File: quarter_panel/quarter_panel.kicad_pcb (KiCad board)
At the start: 2 copper layers, 20 x 20 mm, 4 parts

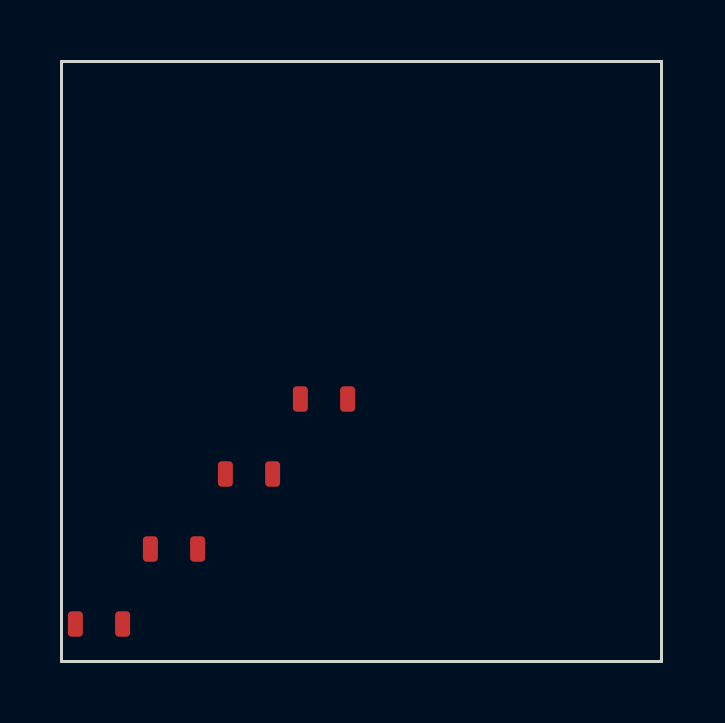
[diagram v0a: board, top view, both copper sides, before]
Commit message: Create new documentation images
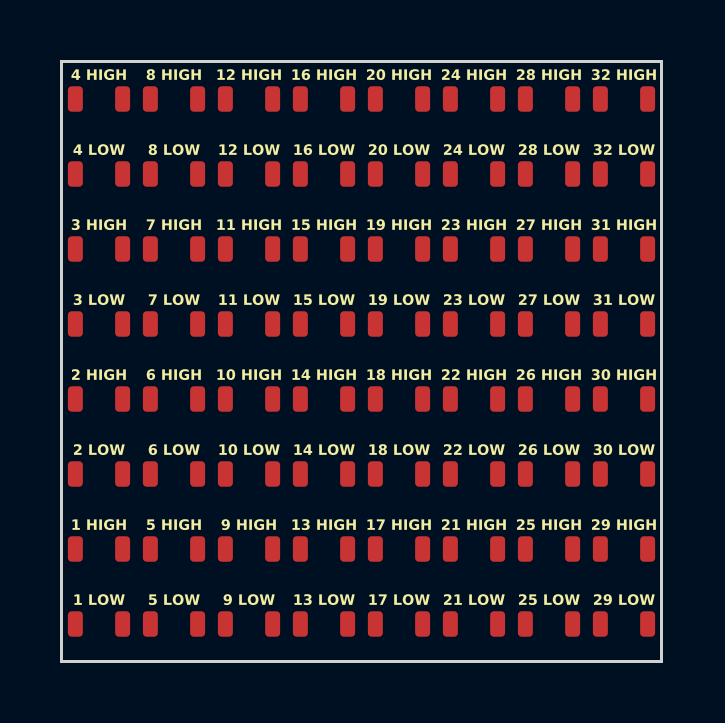
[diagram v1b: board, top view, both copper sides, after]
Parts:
- added REF**: LED_0603_1608Metric, LED_SMD:LED_0603_1608Metric, F.Cu at (128.8, 106.2)
- added REF**: LED_0603_1608Metric, LED_SMD:LED_0603_1608Metric, F.Cu at (138.8, 111.2)
- added REF**: LED_0603_1608Metric, LED_SMD:LED_0603_1608Metric, F.Cu at (138.8, 116.2)
- added REF**: LED_0603_1608Metric, LED_SMD:LED_0603_1608Metric, F.Cu at (131.2, 103.8)
- added REF**: LED_0603_1608Metric, LED_SMD:LED_0603_1608Metric, F.Cu at (143.8, 118.8)
- added REF**: LED_0603_1608Metric, LED_SMD:LED_0603_1608Metric, F.Cu at (143.8, 113.8)
- added REF**: LED_0603_1608Metric, LED_SMD:LED_0603_1608Metric, F.Cu at (133.8, 108.8)
- added REF**: LED_0603_1608Metric, LED_SMD:LED_0603_1608Metric, F.Cu at (128.8, 101.2)
- added REF**: LED_0603_1608Metric, LED_SMD:LED_0603_1608Metric, F.Cu at (136.2, 111.2)
- added REF**: LED_0603_1608Metric, LED_SMD:LED_0603_1608Metric, F.Cu at (131.2, 111.2)
- added REF**: LED_0603_1608Metric, LED_SMD:LED_0603_1608Metric, F.Cu at (138.8, 101.2)
- added REF**: LED_0603_1608Metric, LED_SMD:LED_0603_1608Metric, F.Cu at (133.8, 116.2)
- added REF**: LED_0603_1608Metric, LED_SMD:LED_0603_1608Metric, F.Cu at (141.2, 106.2)
- added REF**: LED_0603_1608Metric, LED_SMD:LED_0603_1608Metric, F.Cu at (131.2, 116.2)
- added REF**: LED_0603_1608Metric, LED_SMD:LED_0603_1608Metric, F.Cu at (143.8, 101.2)
- added REF**: LED_0603_1608Metric, LED_SMD:LED_0603_1608Metric, F.Cu at (143.8, 111.2)
- added REF**: LED_0603_1608Metric, LED_SMD:LED_0603_1608Metric, F.Cu at (133.8, 113.8)
- added REF**: LED_0603_1608Metric, LED_SMD:LED_0603_1608Metric, F.Cu at (143.8, 103.8)
- added REF**: LED_0603_1608Metric, LED_SMD:LED_0603_1608Metric, F.Cu at (143.8, 116.2)
- added REF**: LED_0603_1608Metric, LED_SMD:LED_0603_1608Metric, F.Cu at (126.2, 111.2)
- added REF**: LED_0603_1608Metric, LED_SMD:LED_0603_1608Metric, F.Cu at (133.8, 118.8)
- added REF**: LED_0603_1608Metric, LED_SMD:LED_0603_1608Metric, F.Cu at (126.2, 103.8)
- added REF**: LED_0603_1608Metric, LED_SMD:LED_0603_1608Metric, F.Cu at (141.2, 103.8)
- added REF**: LED_0603_1608Metric, LED_SMD:LED_0603_1608Metric, F.Cu at (131.2, 118.8)
- added REF**: LED_0603_1608Metric, LED_SMD:LED_0603_1608Metric, F.Cu at (128.8, 103.8)
- added REF**: LED_0603_1608Metric, LED_SMD:LED_0603_1608Metric, F.Cu at (141.2, 116.2)
- added REF**: LED_0603_1608Metric, LED_SMD:LED_0603_1608Metric, F.Cu at (143.8, 106.2)
- added REF**: LED_0603_1608Metric, LED_SMD:LED_0603_1608Metric, F.Cu at (131.2, 101.2)
- added REF**: LED_0603_1608Metric, LED_SMD:LED_0603_1608Metric, F.Cu at (141.2, 113.8)
- added REF**: LED_0603_1608Metric, LED_SMD:LED_0603_1608Metric, F.Cu at (138.8, 103.8)
- added REF**: LED_0603_1608Metric, LED_SMD:LED_0603_1608Metric, F.Cu at (136.2, 118.8)
- added REF**: LED_0603_1608Metric, LED_SMD:LED_0603_1608Metric, F.Cu at (128.8, 113.8)
- added REF**: LED_0603_1608Metric, LED_SMD:LED_0603_1608Metric, F.Cu at (128.8, 118.8)
- added REF**: LED_0603_1608Metric, LED_SMD:LED_0603_1608Metric, F.Cu at (138.8, 108.8)
- added REF**: LED_0603_1608Metric, LED_SMD:LED_0603_1608Metric, F.Cu at (141.2, 108.8)
- added REF**: LED_0603_1608Metric, LED_SMD:LED_0603_1608Metric, F.Cu at (141.2, 118.8)
- added REF**: LED_0603_1608Metric, LED_SMD:LED_0603_1608Metric, F.Cu at (131.2, 108.8)
- added REF**: LED_0603_1608Metric, LED_SMD:LED_0603_1608Metric, F.Cu at (141.2, 101.2)
- added REF**: LED_0603_1608Metric, LED_SMD:LED_0603_1608Metric, F.Cu at (126.2, 101.2)
- added REF**: LED_0603_1608Metric, LED_SMD:LED_0603_1608Metric, F.Cu at (143.8, 108.8)
- added REF**: LED_0603_1608Metric, LED_SMD:LED_0603_1608Metric, F.Cu at (141.2, 111.2)
- added REF**: LED_0603_1608Metric, LED_SMD:LED_0603_1608Metric, F.Cu at (136.2, 103.8)
- added REF**: LED_0603_1608Metric, LED_SMD:LED_0603_1608Metric, F.Cu at (128.8, 108.8)
- added REF**: LED_0603_1608Metric, LED_SMD:LED_0603_1608Metric, F.Cu at (138.8, 118.8)
- added REF**: LED_0603_1608Metric, LED_SMD:LED_0603_1608Metric, F.Cu at (133.8, 101.2)
- added REF**: LED_0603_1608Metric, LED_SMD:LED_0603_1608Metric, F.Cu at (138.8, 106.2)
- added REF**: LED_0603_1608Metric, LED_SMD:LED_0603_1608Metric, F.Cu at (128.8, 111.2)
- added REF**: LED_0603_1608Metric, LED_SMD:LED_0603_1608Metric, F.Cu at (131.2, 106.2)
- added REF**: LED_0603_1608Metric, LED_SMD:LED_0603_1608Metric, F.Cu at (133.8, 103.8)
- added REF**: LED_0603_1608Metric, LED_SMD:LED_0603_1608Metric, F.Cu at (136.2, 101.2)
- added REF**: LED_0603_1608Metric, LED_SMD:LED_0603_1608Metric, F.Cu at (126.2, 106.2)
- added REF**: LED_0603_1608Metric, LED_SMD:LED_0603_1608Metric, F.Cu at (126.2, 113.8)
- added REF**: LED_0603_1608Metric, LED_SMD:LED_0603_1608Metric, F.Cu at (126.2, 116.2)
- added REF**: LED_0603_1608Metric, LED_SMD:LED_0603_1608Metric, F.Cu at (136.2, 106.2)
- added REF**: LED_0603_1608Metric, LED_SMD:LED_0603_1608Metric, F.Cu at (136.2, 113.8)
- added REF**: LED_0603_1608Metric, LED_SMD:LED_0603_1608Metric, F.Cu at (136.2, 108.8)
- added REF**: LED_0603_1608Metric, LED_SMD:LED_0603_1608Metric, F.Cu at (133.8, 106.2)
- added REF**: LED_0603_1608Metric, LED_SMD:LED_0603_1608Metric, F.Cu at (126.2, 108.8)
- added REF**: LED_0603_1608Metric, LED_SMD:LED_0603_1608Metric, F.Cu at (136.2, 116.2)
- added REF**: LED_0603_1608Metric, LED_SMD:LED_0603_1608Metric, F.Cu at (138.8, 113.8)

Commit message: Update pixel numbering
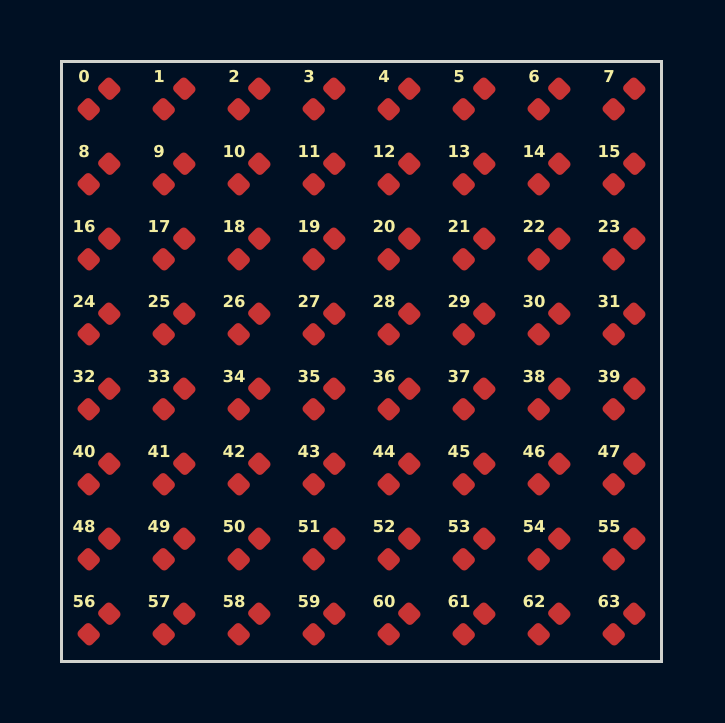
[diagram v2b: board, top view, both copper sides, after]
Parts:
- removed the REF** at (128.8, 106.2)
- removed the REF** at (138.8, 111.2)
- removed the REF** at (138.8, 116.2)
- removed the REF** at (131.2, 103.8)
- removed the REF** at (126.2, 118.8)
- removed the REF** at (143.8, 118.8)
- removed the REF** at (143.8, 113.8)
- removed the REF** at (133.8, 108.8)
- removed the REF** at (128.8, 101.2)
- removed the REF** at (136.2, 111.2)
- removed the REF** at (131.2, 111.2)
- removed the REF** at (138.8, 101.2)
- removed the REF** at (133.8, 116.2)
- removed the REF** at (141.2, 106.2)
- removed the REF** at (131.2, 116.2)
- removed the REF** at (143.8, 101.2)
- removed the REF** at (143.8, 111.2)
- removed the REF** at (133.8, 113.8)
- removed the REF** at (143.8, 103.8)
- removed the REF** at (143.8, 116.2)
- removed the REF** at (126.2, 111.2)
- removed the REF** at (133.8, 118.8)
- removed the REF** at (128.8, 116.2)
- removed the REF** at (126.2, 103.8)
- removed the REF** at (141.2, 103.8)
- removed the REF** at (131.2, 118.8)
- removed the REF** at (128.8, 103.8)
- removed the REF** at (141.2, 116.2)
- removed the REF** at (131.2, 113.8)
- removed the REF** at (143.8, 106.2)
- removed the REF** at (131.2, 101.2)
- removed the REF** at (141.2, 113.8)
- removed the REF** at (138.8, 103.8)
- removed the REF** at (136.2, 118.8)
- removed the REF** at (128.8, 113.8)
- removed the REF** at (128.8, 118.8)
- removed the REF** at (138.8, 108.8)
- removed the REF** at (141.2, 108.8)
- removed the REF** at (141.2, 118.8)
- removed the REF** at (131.2, 108.8)
- removed the REF** at (141.2, 101.2)
- removed the REF** at (126.2, 101.2)
- removed the REF** at (143.8, 108.8)
- removed the REF** at (141.2, 111.2)
- removed the REF** at (136.2, 103.8)
- removed the REF** at (128.8, 108.8)
- removed the REF** at (138.8, 118.8)
- removed the REF** at (133.8, 101.2)
- removed the REF** at (138.8, 106.2)
- removed the REF** at (128.8, 111.2)
- removed the REF** at (131.2, 106.2)
- removed the REF** at (133.8, 103.8)
- removed the REF** at (136.2, 101.2)
- removed the REF** at (126.2, 106.2)
- removed the REF** at (126.2, 113.8)
- removed the REF** at (133.8, 111.2)
- removed the REF** at (126.2, 116.2)
- removed the REF** at (136.2, 106.2)
- removed the REF** at (136.2, 113.8)
- removed the REF** at (136.2, 108.8)
- removed the REF** at (133.8, 106.2)
- removed the REF** at (126.2, 108.8)
- removed the REF** at (136.2, 116.2)
- removed the REF** at (138.8, 113.8)
- added REF**: LED_0402_1005Metric, LED_SMD:LED_0402_1005Metric, F.Cu at (131.2, 103.8)
- added REF**: LED_0402_1005Metric, LED_SMD:LED_0402_1005Metric, F.Cu at (131.2, 106.2)
- added REF**: LED_0402_1005Metric, LED_SMD:LED_0402_1005Metric, F.Cu at (138.8, 118.8)
- added REF**: LED_0402_1005Metric, LED_SMD:LED_0402_1005Metric, F.Cu at (141.2, 113.8)
- added REF**: LED_0402_1005Metric, LED_SMD:LED_0402_1005Metric, F.Cu at (133.8, 108.8)
- added REF**: LED_0402_1005Metric, LED_SMD:LED_0402_1005Metric, F.Cu at (136.2, 106.2)
- added REF**: LED_0402_1005Metric, LED_SMD:LED_0402_1005Metric, F.Cu at (136.2, 118.8)
- added REF**: LED_0402_1005Metric, LED_SMD:LED_0402_1005Metric, F.Cu at (126.2, 103.8)
- added REF**: LED_0402_1005Metric, LED_SMD:LED_0402_1005Metric, F.Cu at (141.2, 118.8)
- added REF**: LED_0402_1005Metric, LED_SMD:LED_0402_1005Metric, F.Cu at (131.2, 118.8)
- added REF**: LED_0402_1005Metric, LED_SMD:LED_0402_1005Metric, F.Cu at (143.8, 103.8)
- added REF**: LED_0402_1005Metric, LED_SMD:LED_0402_1005Metric, F.Cu at (136.2, 116.2)
- added REF**: LED_0402_1005Metric, LED_SMD:LED_0402_1005Metric, F.Cu at (143.8, 116.2)
- added REF**: LED_0402_1005Metric, LED_SMD:LED_0402_1005Metric, F.Cu at (141.2, 103.8)
- added REF**: LED_0402_1005Metric, LED_SMD:LED_0402_1005Metric, F.Cu at (143.8, 118.8)
- added REF**: LED_0402_1005Metric, LED_SMD:LED_0402_1005Metric, F.Cu at (133.8, 106.2)
- added REF**: LED_0402_1005Metric, LED_SMD:LED_0402_1005Metric, F.Cu at (138.8, 106.2)
- added REF**: LED_0402_1005Metric, LED_SMD:LED_0402_1005Metric, F.Cu at (138.8, 108.8)
- added REF**: LED_0402_1005Metric, LED_SMD:LED_0402_1005Metric, F.Cu at (128.8, 111.2)
- added REF**: LED_0402_1005Metric, LED_SMD:LED_0402_1005Metric, F.Cu at (143.8, 101.2)
- added REF**: LED_0402_1005Metric, LED_SMD:LED_0402_1005Metric, F.Cu at (131.2, 108.8)
- added REF**: LED_0402_1005Metric, LED_SMD:LED_0402_1005Metric, F.Cu at (128.8, 101.2)
- added REF**: LED_0402_1005Metric, LED_SMD:LED_0402_1005Metric, F.Cu at (133.8, 101.2)
- added REF**: LED_0402_1005Metric, LED_SMD:LED_0402_1005Metric, F.Cu at (126.2, 101.2)
- added REF**: LED_0402_1005Metric, LED_SMD:LED_0402_1005Metric, F.Cu at (126.2, 106.2)
- added REF**: LED_0402_1005Metric, LED_SMD:LED_0402_1005Metric, F.Cu at (136.2, 111.2)
- added REF**: LED_0402_1005Metric, LED_SMD:LED_0402_1005Metric, F.Cu at (133.8, 118.8)
- added REF**: LED_0402_1005Metric, LED_SMD:LED_0402_1005Metric, F.Cu at (126.2, 116.2)
- added REF**: LED_0402_1005Metric, LED_SMD:LED_0402_1005Metric, F.Cu at (143.8, 108.8)
- added REF**: LED_0402_1005Metric, LED_SMD:LED_0402_1005Metric, F.Cu at (126.2, 108.8)
- added REF**: LED_0402_1005Metric, LED_SMD:LED_0402_1005Metric, F.Cu at (141.2, 101.2)
- added REF**: LED_0402_1005Metric, LED_SMD:LED_0402_1005Metric, F.Cu at (136.2, 103.8)
- added REF**: LED_0402_1005Metric, LED_SMD:LED_0402_1005Metric, F.Cu at (136.2, 101.2)
- added REF**: LED_0402_1005Metric, LED_SMD:LED_0402_1005Metric, F.Cu at (136.2, 113.8)
- added REF**: LED_0402_1005Metric, LED_SMD:LED_0402_1005Metric, F.Cu at (136.2, 108.8)
- added REF**: LED_0402_1005Metric, LED_SMD:LED_0402_1005Metric, F.Cu at (141.2, 106.2)
- added REF**: LED_0402_1005Metric, LED_SMD:LED_0402_1005Metric, F.Cu at (131.2, 111.2)
- added REF**: LED_0402_1005Metric, LED_SMD:LED_0402_1005Metric, F.Cu at (131.2, 101.2)
- added REF**: LED_0402_1005Metric, LED_SMD:LED_0402_1005Metric, F.Cu at (128.8, 113.8)
- added REF**: LED_0402_1005Metric, LED_SMD:LED_0402_1005Metric, F.Cu at (131.2, 116.2)
- added REF**: LED_0402_1005Metric, LED_SMD:LED_0402_1005Metric, F.Cu at (141.2, 116.2)
- added REF**: LED_0402_1005Metric, LED_SMD:LED_0402_1005Metric, F.Cu at (138.8, 101.2)
- added REF**: LED_0402_1005Metric, LED_SMD:LED_0402_1005Metric, F.Cu at (138.8, 103.8)
- added REF**: LED_0402_1005Metric, LED_SMD:LED_0402_1005Metric, F.Cu at (128.8, 118.8)
- added REF**: LED_0402_1005Metric, LED_SMD:LED_0402_1005Metric, F.Cu at (133.8, 116.2)
- added REF**: LED_0402_1005Metric, LED_SMD:LED_0402_1005Metric, F.Cu at (131.2, 113.8)
- added REF**: LED_0402_1005Metric, LED_SMD:LED_0402_1005Metric, F.Cu at (138.8, 111.2)
- added REF**: LED_0402_1005Metric, LED_SMD:LED_0402_1005Metric, F.Cu at (138.8, 116.2)
- added REF**: LED_0402_1005Metric, LED_SMD:LED_0402_1005Metric, F.Cu at (126.2, 111.2)
- added REF**: LED_0402_1005Metric, LED_SMD:LED_0402_1005Metric, F.Cu at (143.8, 113.8)
- added REF**: LED_0402_1005Metric, LED_SMD:LED_0402_1005Metric, F.Cu at (128.8, 103.8)
- added REF**: LED_0402_1005Metric, LED_SMD:LED_0402_1005Metric, F.Cu at (128.8, 108.8)
- added REF**: LED_0402_1005Metric, LED_SMD:LED_0402_1005Metric, F.Cu at (128.8, 116.2)
- added REF**: LED_0402_1005Metric, LED_SMD:LED_0402_1005Metric, F.Cu at (143.8, 111.2)
- added REF**: LED_0402_1005Metric, LED_SMD:LED_0402_1005Metric, F.Cu at (128.8, 106.2)
- added REF**: LED_0402_1005Metric, LED_SMD:LED_0402_1005Metric, F.Cu at (126.2, 113.8)
- added REF**: LED_0402_1005Metric, LED_SMD:LED_0402_1005Metric, F.Cu at (133.8, 103.8)
- added REF**: LED_0402_1005Metric, LED_SMD:LED_0402_1005Metric, F.Cu at (133.8, 113.8)
- added REF**: LED_0402_1005Metric, LED_SMD:LED_0402_1005Metric, F.Cu at (126.2, 118.8)
- added REF**: LED_0402_1005Metric, LED_SMD:LED_0402_1005Metric, F.Cu at (133.8, 111.2)
- added REF**: LED_0402_1005Metric, LED_SMD:LED_0402_1005Metric, F.Cu at (138.8, 113.8)
- added REF**: LED_0402_1005Metric, LED_SMD:LED_0402_1005Metric, F.Cu at (143.8, 106.2)
- added REF**: LED_0402_1005Metric, LED_SMD:LED_0402_1005Metric, F.Cu at (141.2, 108.8)
- added REF**: LED_0402_1005Metric, LED_SMD:LED_0402_1005Metric, F.Cu at (141.2, 111.2)

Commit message: Update names and documentation
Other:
- board text added: "Bit 0"
- board text added: "Bit 0:3"
- board text added: "Bit 1"
- board text added: "Bit 2"
- board text added: "Bit 3"
- board text added: "Bit 4"
- board text added: "Bit 4:7"
- board text added: "Bit 5"
- board text added: "Bit 6"
- board text added: "Bit 7"
- board text added: "Byte 1"
- board text added: "Byte 10"
- board text added: "Byte 11"
- board text added: "Byte 12"
- board text added: "Byte 13"
- board text added: "Byte 14"
- board text added: "Byte 15"
- board text added: "Byte 16"
- board text added: "Byte 17"
- board text added: "Byte 18"
- board text added: "Byte 19"
- board text added: "Byte 2"
- board text added: "Byte 20"
- board text added: "Byte 21"
- board text added: "Byte 22"
- board text added: "Byte 23"
- board text added: "Byte 24"
- board text added: "Byte 25"
- board text added: "Byte 26"
- board text added: "Byte 27"
- board text added: "Byte 28"
- board text added: "Byte 29"
- board text added: "Byte 3"
- board text added: "Byte 30"
- board text added: "Byte 31"
- board text added: "Byte 32"
- board text added: "Byte 4"
- board text added: "Byte 5"
- board text added: "Byte 6"
- board text added: "Byte 7"
- board text added: "Byte 8"
- board text added: "Byte 9"
